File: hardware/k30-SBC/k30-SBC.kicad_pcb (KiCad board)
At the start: 2 copper layers, 0 parts

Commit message: Almost completed k30-SBC board design
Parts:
- added C1: 0.47uF, Capacitor_THT:C_Disc_D3.0mm_W2.0mm_P2.50mm, F.Cu at (54.6, 44.4)
- added C10: 0.1uF, Capacitor_THT:C_Disc_D3.0mm_W2.0mm_P2.50mm, F.Cu at (160.0, 53.7)
- added C11: 0.1uF, Capacitor_THT:C_Disc_D3.0mm_W2.0mm_P2.50mm, F.Cu at (132.1, 65.4)
- added C12: 0.1uF, Capacitor_THT:C_Disc_D3.0mm_W2.0mm_P2.50mm, F.Cu at (122.4, 65.4)
- added C13: 0.1uF, Capacitor_THT:C_Disc_D3.0mm_W2.0mm_P2.50mm, F.Cu at (150.4, 65.4)
- added C14: 0.1uF, Capacitor_THT:C_Disc_D3.0mm_W2.0mm_P2.50mm, F.Cu at (141.2, 65.4)
- added C15: 0.1uF, Capacitor_THT:C_Disc_D3.0mm_W2.0mm_P2.50mm, F.Cu at (167.6, 65.4)
- added C16: 0.1uF, Capacitor_THT:C_Disc_D3.0mm_W2.0mm_P2.50mm, F.Cu at (160.0, 65.4)
- added C17: 0.1uF, Capacitor_THT:C_Disc_D3.0mm_W2.0mm_P2.50mm, F.Cu at (91.4, 52.1)
- added C18: 0.1uF, Capacitor_THT:C_Disc_D3.0mm_W2.0mm_P2.50mm, F.Cu at (128.3, 100.1)
- added C19: 0.1uF, Capacitor_THT:C_Disc_D3.0mm_W2.0mm_P2.50mm, F.Cu at (148.6, 100.1)
- added C2: 15pF, Capacitor_THT:C_Disc_D3.0mm_W2.0mm_P2.50mm, F.Cu at (90.4, 83.9)
- added C20: 0.1uF, Capacitor_THT:C_Disc_D3.0mm_W2.0mm_P2.50mm, F.Cu at (151.1, 105.9)
- added C3: 5pF, Capacitor_THT:C_Disc_D3.0mm_W2.0mm_P2.50mm, F.Cu at (74.5, 83.9)
- added C4: 0.1uF, Capacitor_THT:C_Disc_D3.0mm_W2.0mm_P2.50mm, F.Cu at (132.1, 53.7)
- added C5: 0.1uF, Capacitor_THT:C_Disc_D3.0mm_W2.0mm_P2.50mm, F.Cu at (71.1, 99.1)
- added C6: 0.1uF, Capacitor_THT:C_Disc_D3.0mm_W2.0mm_P2.50mm, F.Cu at (151.4, 53.7)
- added C7: 0.1uF, Capacitor_THT:C_Disc_D3.0mm_W2.0mm_P2.50mm, F.Cu at (141.7, 53.7)
- added C8: 470uF, Capacitor_THT:CP_Radial_D8.0mm_P5.00mm, F.Cu at (157.0, 42.7)
- added C9: 0.1uF, Capacitor_THT:C_Disc_D3.0mm_W2.0mm_P2.50mm, F.Cu at (169.7, 53.7)
- added D1: HALT, LED_THT:LED_D5.0mm, F.Cu at (42.5, 52.1)
- added D2: OP5, LED_THT:LED_D5.0mm, F.Cu at (52.7, 83.8)
- added D3: OP7, LED_THT:LED_D5.0mm, F.Cu at (42.5, 83.8)
- added D4: OP4, LED_THT:LED_D5.0mm, F.Cu at (52.7, 76.2)
- added D5: OP6, LED_THT:LED_D5.0mm, F.Cu at (42.5, 76.2)
- added J1: CompactFlash, 68k-SMT:CF-Card_3M_N7E50-Q516RB-40, F.Cu at (61.0, 113.0)
- added J2: Serial1, Connector_PinHeader_2.54mm:PinHeader_1x06_P2.54mm_Horizontal, F.Cu at (82.5, 43.8)
- added J3: Serial2, Connector_PinHeader_2.54mm:PinHeader_1x06_P2.54mm_Horizontal, F.Cu at (62.9, 43.8)
- added J4: ADBUS-EXP, Connector_PinHeader_2.54mm:PinHeader_2x15_P2.54mm_Vertical, F.Cu at (191.8, 41.9)
- added J5: ADBUS, Connector_PinHeader_2.54mm:PinHeader_2x20_P2.54mm_Vertical, F.Cu at (191.8, 85.1)
- added J6: SIGBUS, Connector_PinHeader_2.54mm:PinHeader_2x20_P2.54mm_Vertical, F.Cu at (179.1, 41.9)
- added J7: POWER, Connector_PinHeader_2.54mm:PinHeader_1x02_P2.54mm_Vertical, F.Cu at (143.1, 41.1)
- added J8: POWER, Connector_PinHeader_2.54mm:PinHeader_1x02_P2.54mm_Vertical, F.Cu at (147.6, 41.1)
- added J9: POWER, Connector_PinHeader_2.54mm:PinHeader_1x02_P2.54mm_Vertical, F.Cu at (152.0, 41.1)
- added JP1: ROMJMP, Connector_PinHeader_2.54mm:PinHeader_1x03_P2.54mm_Vertical, F.Cu at (173.7, 69.8)
- added JP2: IRQ, Connector_PinHeader_2.54mm:PinHeader_1x02_P2.54mm_Vertical, F.Cu at (101.0, 43.2)
- added JP3: IACK, Connector_PinHeader_2.54mm:PinHeader_1x02_P2.54mm_Vertical, F.Cu at (105.0, 43.2)
- added JP4: POWER, Connector_PinHeader_2.54mm:PinHeader_1x02_P2.54mm_Vertical, F.Cu at (86.4, 48.9)
- added JP5: POWER, Connector_PinHeader_2.54mm:PinHeader_1x02_P2.54mm_Vertical, F.Cu at (66.7, 48.9)
- added R1: 1k, Resistor_THT:R_Axial_DIN0204_L3.6mm_D1.6mm_P5.08mm_Horizontal, F.Cu at (48.9, 54.6)
- added R10: 1k, Resistor_THT:R_Axial_DIN0204_L3.6mm_D1.6mm_P5.08mm_Horizontal, F.Cu at (59.1, 78.7)
- added R11: 1k, Resistor_THT:R_Axial_DIN0204_L3.6mm_D1.6mm_P5.08mm_Horizontal, F.Cu at (48.9, 78.7)
- added R2: 1k, Resistor_THT:R_Axial_DIN0204_L3.6mm_D1.6mm_P5.08mm_Horizontal, F.Cu at (51.4, 49.5)
- added R3: 10k, Resistor_THT:R_Axial_DIN0204_L3.6mm_D1.6mm_P5.08mm_Horizontal, F.Cu at (51.4, 40.6)
- added R4: 5.1k, Resistor_THT:R_Axial_DIN0204_L3.6mm_D1.6mm_P5.08mm_Horizontal, F.Cu at (109.3, 56.5)
- added R5: 5.1k, Resistor_THT:R_Axial_DIN0204_L3.6mm_D1.6mm_P5.08mm_Horizontal, F.Cu at (116.5, 56.5)
- added R6: 10k, Resistor_THT:R_Axial_DIN0204_L3.6mm_D1.6mm_P5.08mm_Horizontal, F.Cu at (54.6, 61.0)
- added R7: 1k, Resistor_THT:R_Axial_DIN0204_L3.6mm_D1.6mm_P5.08mm_Horizontal, F.Cu at (59.1, 86.4)
- added R8: 1k, Resistor_THT:R_Axial_DIN0204_L3.6mm_D1.6mm_P5.08mm_Horizontal, F.Cu at (48.9, 86.4)
- added R9: 10k, Resistor_THT:R_Axial_DIN0204_L3.6mm_D1.6mm_P5.08mm_Horizontal, F.Cu at (42.5, 61.0)
- added RN1: 10k, Resistor_THT:R_Array_SIP9, F.Cu at (77.5, 90.2)
- added RN2: 10k, Resistor_THT:R_Array_SIP9, F.Cu at (77.5, 94.6)
- added SW1: RESET, Button_Switch_THT:SW_PUSH_6mm, F.Cu at (41.9, 41.2)
- added SW2: SW_DIP_x06, Package_DIP:DIP-12_W7.62mm_LongPads, F.Cu at (111.3, 47.8)
- added SW3: IP2, Button_Switch_THT:SW_PUSH_6mm, F.Cu at (41.9, 64.1)
- added SW4: IP3, Button_Switch_THT:SW_PUSH_6mm, F.Cu at (54.0, 64.1)
- added TP1: IPEND, TestPoint:TestPoint_THTPad_2.0x2.0mm_Drill1.0mm, F.Cu at (77.7, 135.6)
- added TP2: REFILL, TestPoint:TestPoint_THTPad_2.0x2.0mm_Drill1.0mm, F.Cu at (82.3, 135.6)
- added TP3: STATUS, TestPoint:TestPoint_THTPad_2.0x2.0mm_Drill1.0mm, F.Cu at (86.9, 135.6)
- added TP4: DSACK-EXT, TestPoint:TestPoint_THTPad_2.0x2.0mm_Drill1.0mm, F.Cu at (130.6, 43.1)
- added TP5: IP3, TestPoint:TestPoint_THTPad_2.0x2.0mm_Drill1.0mm, F.Cu at (62.9, 59.7)
- added TP6: IP2, TestPoint:TestPoint_THTPad_2.0x2.0mm_Drill1.0mm, F.Cu at (50.8, 59.7)
- added U1: MC68030FE, Package_QFP:PQFP-132_24x24mm_P0.635mm, F.Cu at (90.2, 115.0)
- added U10: 74HC253, Package_SO:SSOP-16_3.9x4.9mm_P0.635mm, F.Cu at (147.4, 70.7)
- added U11: 74HC138, Package_SO:TSSOP-16_4.4x5mm_P0.65mm, F.Cu at (166.4, 70.7)
- added U12: 74HC393, Package_SO:TSSOP-14_4.4x5mm_P0.65mm, F.Cu at (148.2, 58.7)
- added U13: MC68681, Package_LCC:PLCC-44_THT-Socket, F.Cu at (84.2, 60.1)
- added U14: AS6C8016, Package_SO:TSOP-II-44_10.16x18.41mm_P0.8mm, F.Cu at (120.0, 109.8)
- added U15: AS6C8016, Package_SO:TSOP-II-44_10.16x18.41mm_P0.8mm, F.Cu at (139.1, 109.9)
- added U16: AM29F040, Package_LCC:PLCC-32_THT-Socket, F.Cu at (159.4, 108.6)
- added U2: 74HC14, Package_SO:TSSOP-14_4.4x5mm_P0.65mm, F.Cu at (128.8, 58.7)
- added U3: 74HC05, Package_SO:TSSOP-14_4.4x5mm_P0.65mm, F.Cu at (138.5, 58.7)
- added U4: 74HC139, Package_SO:TSSOP-16_4.4x5mm_P0.65mm, F.Cu at (119.2, 70.7)
- added U5: 4072, Package_SO:TSSOP-14_4.4x5mm_P0.65mm, F.Cu at (156.8, 70.4)
- added U6: 74HC20, Package_SO:TSSOP-14_4.4x5mm_P0.65mm, F.Cu at (166.4, 58.7)
- added U7: 74HC32, Package_SO:TSSOP-14_4.4x5mm_P0.65mm, F.Cu at (157.3, 58.7)
- added U8: 74HC08, Package_SO:TSSOP-14_4.4x5mm_P0.65mm, F.Cu at (128.8, 70.4)
- added U9: 74HC253, Package_SO:SSOP-16_3.9x4.9mm_P0.635mm, F.Cu at (138.2, 70.7)
- added Y1: Crystal, Crystal:Crystal_HC49-4H_Vertical, F.Cu at (113.1, 60.9)
- added Y2: Crystal, Crystal:Crystal_HC49-4H_Vertical, F.Cu at (80.1, 82.9)
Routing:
- net A1: track 0.00 -> 363.4 mm, vias 0 -> 6
- net A2: track 0.00 -> 296.7 mm, vias 0 -> 5
- net A3: track 0.00 -> 293.7 mm, vias 0 -> 5
- net A4: track 0.00 -> 291.5 mm, vias 0 -> 6
- net D25: track 0.00 -> 267.9 mm, vias 0 -> 5
- net A0: track 0.00 -> 264.0 mm, vias 0 -> 4
- net A31: track 0.00 -> 259.3 mm, vias 0 -> 4
- net D24: track 0.00 -> 258.0 mm, vias 0 -> 5
- net A30: track 0.00 -> 256.0 mm, vias 0 -> 4
- net A29: track 0.00 -> 255.9 mm, vias 0 -> 4
- net A27: track 0.00 -> 254.2 mm, vias 0 -> 4
- net WR: track 0.00 -> 254.1 mm, vias 0 -> 6
- net A28: track 0.00 -> 253.3 mm, vias 0 -> 4
- net D26: track 0.00 -> 252.7 mm, vias 0 -> 5
- net D27: track 0.00 -> 247.5 mm, vias 0 -> 5
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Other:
- board outline added: 160 x 100 mm
- copper layers 2 -> 4
- net class Default: via_dia 0.6 -> 0.45; via_drill 0.3 -> 0.2
- net class Narrow added: clearance 0.127, trace_width 0.127, via_dia 0.45, via_drill 0.2
- rule via_min_drill: 0.3 -> 0.2
- rule via_min_size: 0.6 -> 0.45

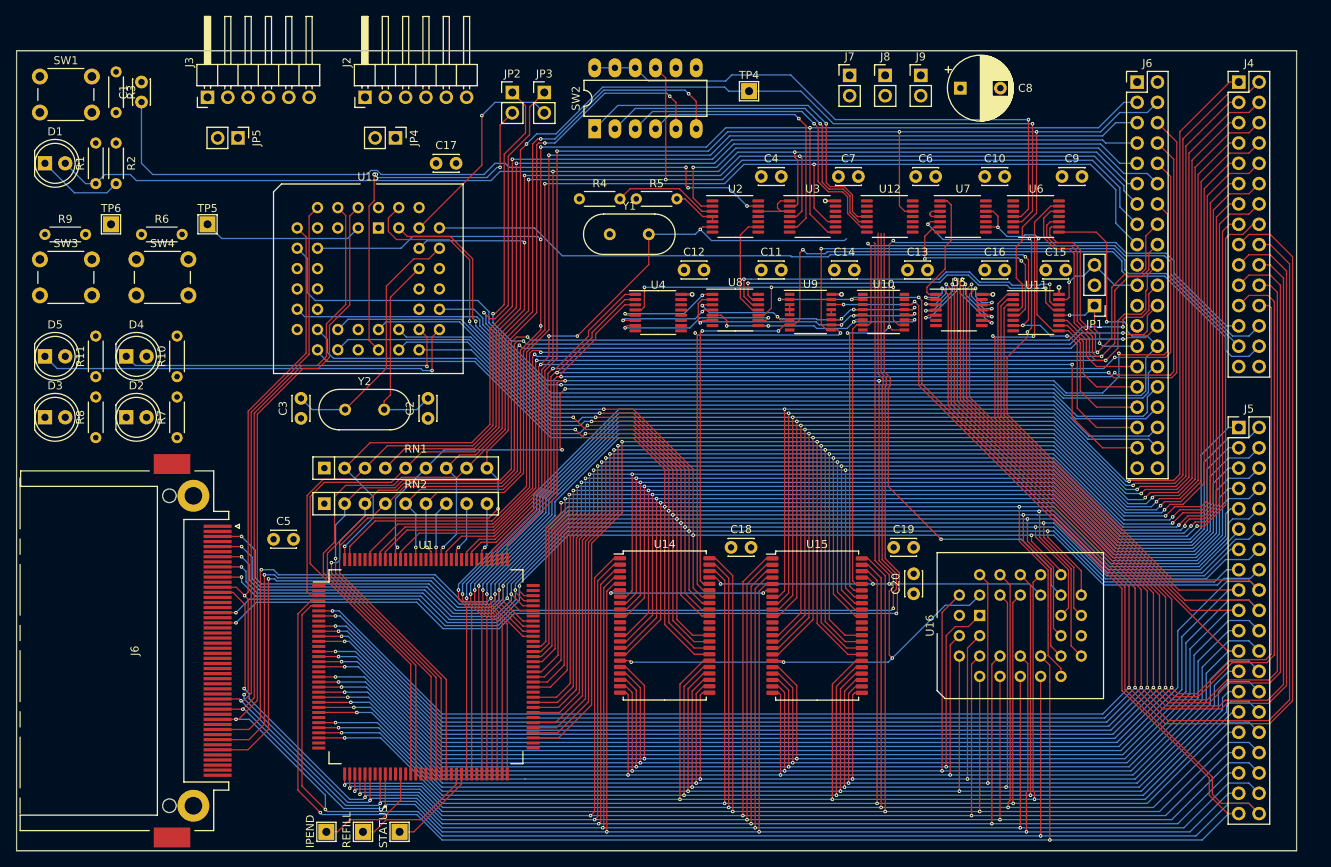
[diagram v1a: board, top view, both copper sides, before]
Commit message: Fixed CF footprint and the wrong data pins going for CF
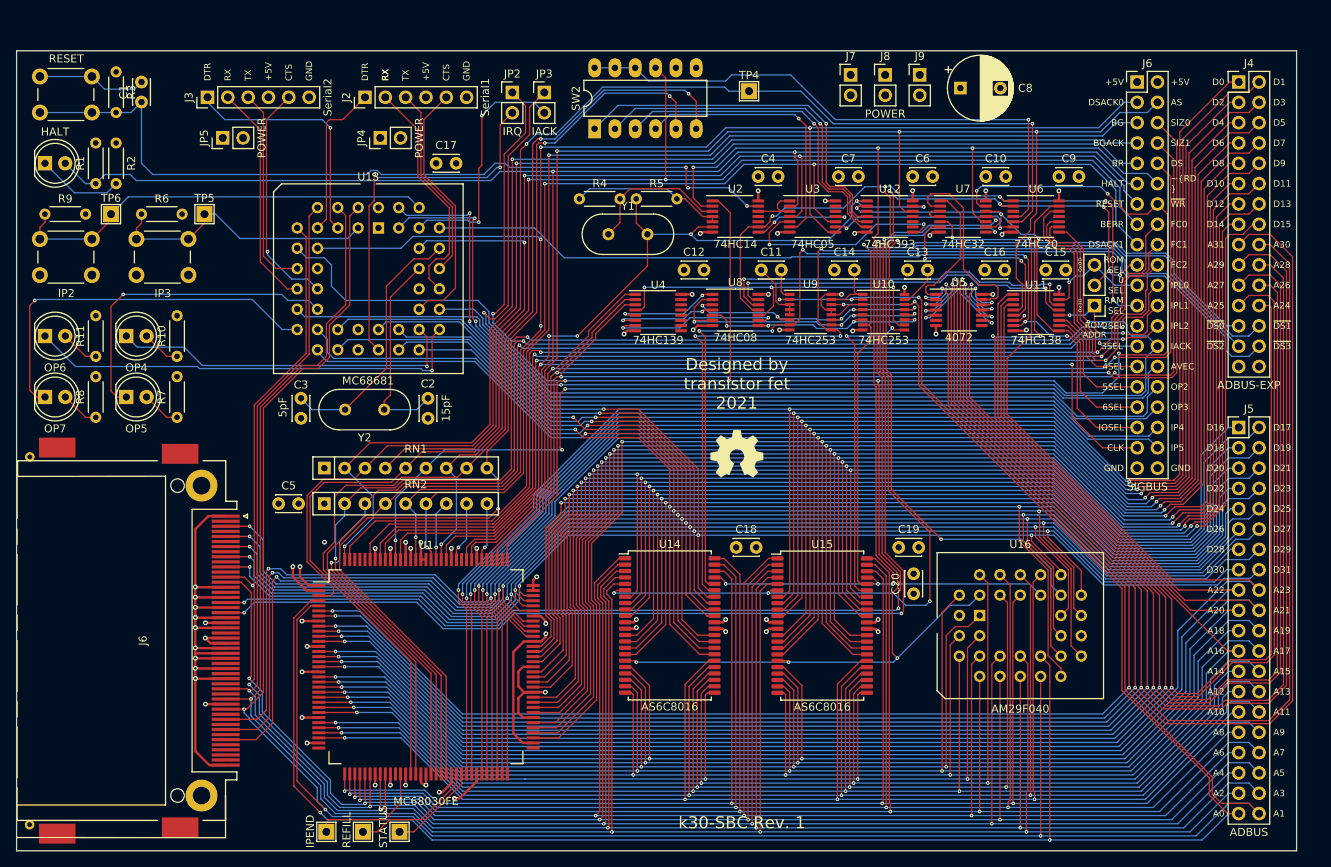
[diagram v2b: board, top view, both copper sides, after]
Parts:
- added REF**: OSHW-Symbol_6.7x6mm_SilkScreen, Symbol:OSHW-Symbol_6.7x6mm_SilkScreen, F.Cu at (129.0, 88.4)
- J2, J3: footprint Connector_PinHeader_2.54mm:PinHeader_1x06_P2.54mm_Horizontal -> Connector_PinHeader_2.54mm:PinHeader_1x06_P2.54mm_Vertical
- moved C5 4.49 mm to (71.8, 94.6)
- moved D4 2.54 mm to (52.7, 73.7)
- moved D5 2.54 mm to (42.5, 73.7)
- moved R7 2.54 mm to (59.1, 83.8)
- moved R8 2.54 mm to (48.9, 83.8)
- moved R6 2.54 mm to (54.6, 58.4)
- moved R9 2.54 mm to (42.5, 58.4)
- moved SW3 2.54 mm to (41.9, 61.5)
- moved SW4 2.54 mm to (54.0, 61.5)
- moved D2 2.54 mm to (52.7, 81.3)
- moved D3 2.54 mm to (42.5, 81.3)
- moved R10 2.54 mm to (59.1, 76.2)
- moved R11 2.54 mm to (48.9, 76.2)
- moved JP4 1.91 mm to (84.5, 48.9), turned to 90 degrees
- moved JP5 1.91 mm to (64.8, 48.9), turned to 90 degrees
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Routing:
- net GND: track 0.00 -> 943.3 mm, vias 0 -> 38
- net +5V: track 71.2 -> 781.1 mm, vias 5 -> 30
- net RAMSEL: track 35.0 -> 175.8 mm, vias 2 -> 8
- net Net-(R9-Pad1): track 0.00 -> 54.0 mm
- net WR: track 254.1 -> 304.5 mm, vias 6 -> 9
- net Net-(D3-Pad1): track 0.00 -> 48.1 mm, vias 0 -> 1
- net ROMSEL: track 66.8 -> 110.5 mm, vias 1 -> 6
- net Net-(D2-Pad1): track 0.00 -> 40.0 mm, vias 0 -> 1
- net Net-(J2-Pad5): track 0.00 -> 32.3 mm
- net Net-(J3-Pad1): track 0.00 -> 30.2 mm, vias 0 -> 1
- net Net-(J2-Pad2): track 0.00 -> 29.5 mm
- net Net-(J3-Pad5): track 0.00 -> 28.9 mm, vias 0 -> 1
- net Net-(J3-Pad2): track 0.00 -> 28.3 mm
- net Net-(U12-Pad8): track 0.00 -> 26.9 mm, vias 0 -> 2
- net Net-(J3-Pad3): track 0.00 -> 25.5 mm
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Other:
- board text added: "+5V"
- board text added: "0 SEL"
- board text added: "0x00"
- board text added: "0x30"
- board text added: "2SEL"
- board text added: "3SEL"
- board text added: "4SEL"
- board text added: "5SEL"
- board text added: "6SEL"
- board text added: "A0"
- board text added: "A1"
- board text added: "A10"
- board text added: "A11"
- board text added: "A12"
- board text added: "A13"
- board text added: "A14"
- board text added: "A15"
- board text added: "A16"
- board text added: "A17"
- board text added: "A18"
- board text added: "A19"
- board text added: "A2"
- board text added: "A20"
- board text added: "A21"
- board text added: "A22"
- board text added: "A23"
- board text added: "A24"
- board text added: "A25"
- board text added: "A26"
- board text added: "A27"
- board text added: "A28"
- board text added: "A29"
- board text added: "A3"
- board text added: "A30"
- board text added: "A31"
- board text added: "A4"
- board text added: "A5"
- board text added: "A6"
- board text added: "A7"
- board text added: "A8"
- board text added: "A9"
- board text added: "AS"
- board text added: "AVEC"
- board text added: "BERR"
- board text added: "BG"
- board text added: "BGACK"
- board text added: "BR"
- board text added: "CLK"
- board text added: "CTS"
- board text added: "D0"
- board text added: "D1"
- board text added: "D10"
- board text added: "D11"
- board text added: "D12"
- board text added: "D13"
- board text added: "D14"
- board text added: "D15"
- board text added: "D16"
- board text added: "D17"
- board text added: "D18"
- board text added: "D19"
- board text added: "D2"
- board text added: "D20"
- board text added: "D21"
- board text added: "D22"
- board text added: "D23"
- board text added: "D24"
- board text added: "D25"
- board text added: "D26"
- board text added: "D27"
- board text added: "D28"
- board text added: "D29"
- board text added: "D3"
- board text added: "D30"
- board text added: "D31"
- board text added: "D4"
- board text added: "D5"
- board text added: "D6"
- board text added: "D7"
- board text added: "D8"
- board text added: "D9"
- board text added: "DS"
- board text added: "DSACK0"
- board text added: "DSACK1"
- board text added: "DTR"
- board text added: "Designed by transistor fet 2021"
- board text added: "FC0"
- board text added: "FC1"
- board text added: "FC2"
- board text added: "GND"
- board text added: "HALT"
- board text added: "IACK"
- board text added: "IOSEL"
- board text added: "IP4"
- board text added: "IP5"
- board text added: "IPL0"
- board text added: "IPL1"
- board text added: "IPL2"
- board text added: "OP2"
- board text added: "OP3"
- board text added: "RAM SEL"
- board text added: "RESET"
- board text added: "ROM ADDR"
- board text added: "ROM SEL"
- board text added: "RX"
- board text added: "SIZ0"
- board text added: "SIZ1"
- board text added: "TX"
- board text added: "k30-SBC Rev. 1"
- board text added: "~DS0"
- board text added: "~DS1"
- board text added: "~DS2"
- board text added: "~DS3"
- board text added: "~RD"
- board text added: "~WR"

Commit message: Last minute changes: swapped WR/DS pins, added testpoint
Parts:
- added TP7: RMC, TestPoint:TestPoint_THTPad_2.0x2.0mm_Drill1.0mm, F.Cu at (73.2, 135.6)
- moved D3 10.2 mm to (52.7, 81.3)
- moved D4 10.2 mm to (42.5, 73.7)
- moved R10 10.2 mm to (48.9, 76.2)
- moved R8 10.2 mm to (59.1, 83.8)
- moved D2 7.62 mm to (52.7, 73.7)
- moved D5 7.62 mm to (42.5, 81.3)
- moved R11 7.62 mm to (48.9, 83.8)
- moved R7 7.62 mm to (59.1, 76.2)
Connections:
- J6 pad 10: DS -> WR
- J6 pad 14: WR -> DS
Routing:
- net Net-(TP7-Pad1): track 0.00 -> 46.8 mm, vias 0 -> 2
- net Net-(D2-Pad1): track 40.0 -> 29.7 mm
- net Net-(D4-Pad1): track 44.2 -> 54.4 mm
- net Net-(D3-Pad1): track 48.1 -> 38.3 mm
- net ~DS3: track 120.1 -> 127.3 mm, vias 3 -> 2
- net DS: track 146.4 -> 140.7 mm
- net WR: track 304.5 -> 309.5 mm
- net ~DS2: track 122.6 -> 126.3 mm, vias 3 -> 2
- net GND: track 943.3 -> 943.2 mm, vias 38 -> 43
- added copper zone on In1.Cu, net +5V
- added copper zone on B.Cu, net GND
- added copper zone on F.Cu, net GND
- added copper zone on In2.Cu, net GND
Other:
- board text added: "16"
- board text added: "4"
- board text added: "8"
- board text added: "CFCARD DELAY (ONLY ONE ON)"
- board text added: "DISABLE CACHE"
- board text added: "DISABLE MMU"
- board text added: "ENABLE BUS ERR"
- board text added: "~0 SEL"
- board text added: "~3SEL"
- board text added: "~4SEL"
- board text added: "~5SEL"
- board text added: "~6SEL"
- board text added: "~AS"
- board text added: "~AVEC"
- board text added: "~BERR"
- board text added: "~BG"
- board text added: "~BGACK"
- board text added: "~BR"
- board text added: "~DS"
- board text added: "~DSACK0"
- board text added: "~DSACK1"
- board text added: "~HALT"
- board text added: "~IACK"
- board text added: "~IOSEL"
- board text added: "~IPL0"
- board text added: "~IPL1"
- board text added: "~IPL2"
- board text added: "~RAM SEL"
- board text added: "~RESET"
- board text added: "~ROM SEL"
- board text removed: "0 SEL"
- board text removed: "2SEL"
- board text removed: "3SEL"
- board text removed: "4SEL"
- board text removed: "5SEL"
- board text removed: "6SEL"
- board text removed: "AS"
- board text removed: "AVEC"
- board text removed: "BERR"
- board text removed: "BG"
- board text removed: "BGACK"
- board text removed: "BR"
- board text removed: "DS"
- board text removed: "DSACK0"
- board text removed: "DSACK1"
- board text removed: "HALT"
- board text removed: "IACK"
- board text removed: "IOSEL"
- board text removed: "IPL0"
- board text removed: "IPL1"
- board text removed: "IPL2"
- board text removed: "RAM SEL"
- board text removed: "RESET"
- board text removed: "ROM SEL"
